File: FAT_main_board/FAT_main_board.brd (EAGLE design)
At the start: 335.3 x 178.7 mm, 42 parts, among them IC1 74LS241N

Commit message: [FAT board] Route board.
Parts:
- removed BAT_POWER1, BAT_POWER2, BAT_SIG1: (no value), con-ptr500:AK300/2
- added 12VSIG, POWER, POWER2: (no value), con-ptr500:AK300/2
- moved BAT_POWER 147.9 mm to (96.5, 1.27), turned to 180 degrees
- moved BAT_SIG 137.7 mm to (81.3, 1.27)
- moved BAU&INT 130.2 mm to (108.0, 1.27), turned to 180 degrees
- moved INTERRUPTOR 126.3 mm to (73.7, 16.5)
- moved BUCK_5V 107.6 mm to (41.9, 10.2), turned to 180 degrees
- moved HB3 85.9 mm to (20.3, 59.7), turned to 90 degrees
- moved C4 85.4 mm to (99.1, 58.4), turned to 0 degrees
- moved BUCK_10V 73.1 mm to (99.1, 29.2), turned to 90 degrees
- moved C6 63.2 mm to (26.7, 72.4), turned to 180 degrees
- moved C5 55.3 mm to (26.7, 47.0), turned to 0 degrees
- moved R3 45.8 mm to (41.9, 33.0), turned to 0 degrees
- moved DYN3 41.0 mm to (66.0, 29.2), turned to 90 degrees
- moved MOTOR3 40.7 mm to (36.8, 59.7), turned to 90 degrees
- moved JP2 40.6 mm to (52.1, 41.9), turned to 270 degrees
- moved DYN2 31.8 mm to (73.7, 29.2), turned to 90 degrees
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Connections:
- removed net N$22: BUCK_5V.IN+, INTERRUPTOR.1
- removed net N$23: BAT_POWER.2, BAT_POWER1.2, BAT_POWER2.2, BUCK_10V.IN-
- removed net N$25: BAT_SIG.2, BAT_SIG1.2, BUCK_5V.IN-
- new net 12V_SIG: 12VSIG.1, BUCK_5V.IN+, INTERRUPTOR.1
- net 12V_POWER: now also POWER.1, POWER2.1
- net GND: now also 12VSIG.2, BAT_POWER.2, BAT_SIG.2, BUCK_10V.IN-, BUCK_5V.IN-, POWER.2, POWER2.2
- net N$13: no longer BAT_POWER1.1, BAT_POWER2.1
- net N$18: now also SV2.8
- net N$20: no longer BAT_SIG1.1
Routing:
- net VCC: track 0.00 -> 366.5 mm, vias 0 -> 6
- net 12V_POWER: track 0.00 -> 292.1 mm
- net GND: track 0.00 -> 182.2 mm, vias 0 -> 13
- net MOT3_CURRENT: track 0.00 -> 108.0 mm, vias 0 -> 1
- net N$24: track 0.00 -> 98.6 mm, vias 0 -> 2
- net N$40: track 0.00 -> 55.8 mm
- net MOT3_BRK: track 0.00 -> 55.5 mm, vias 0 -> 1
- net MOT2_PWM: track 0.00 -> 49.0 mm, vias 0 -> 2
- net MOT2_BRK: track 0.00 -> 48.0 mm, vias 0 -> 2
- net N$8: track 0.00 -> 46.4 mm
- net MOT2_DIR: track 0.00 -> 46.2 mm, vias 0 -> 2
- net N$1: track 0.00 -> 43.7 mm, vias 0 -> 2
- net MOT2_CURRENT: track 0.00 -> 43.0 mm, vias 0 -> 2
- net MOT1_CURRENT: track 0.00 -> 42.7 mm
- net N$19: track 0.00 -> 42.5 mm
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- added copper zone on layer 16, net GND
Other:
- board size 335.3 x 178.7 mm -> 381 x 224.5 mm

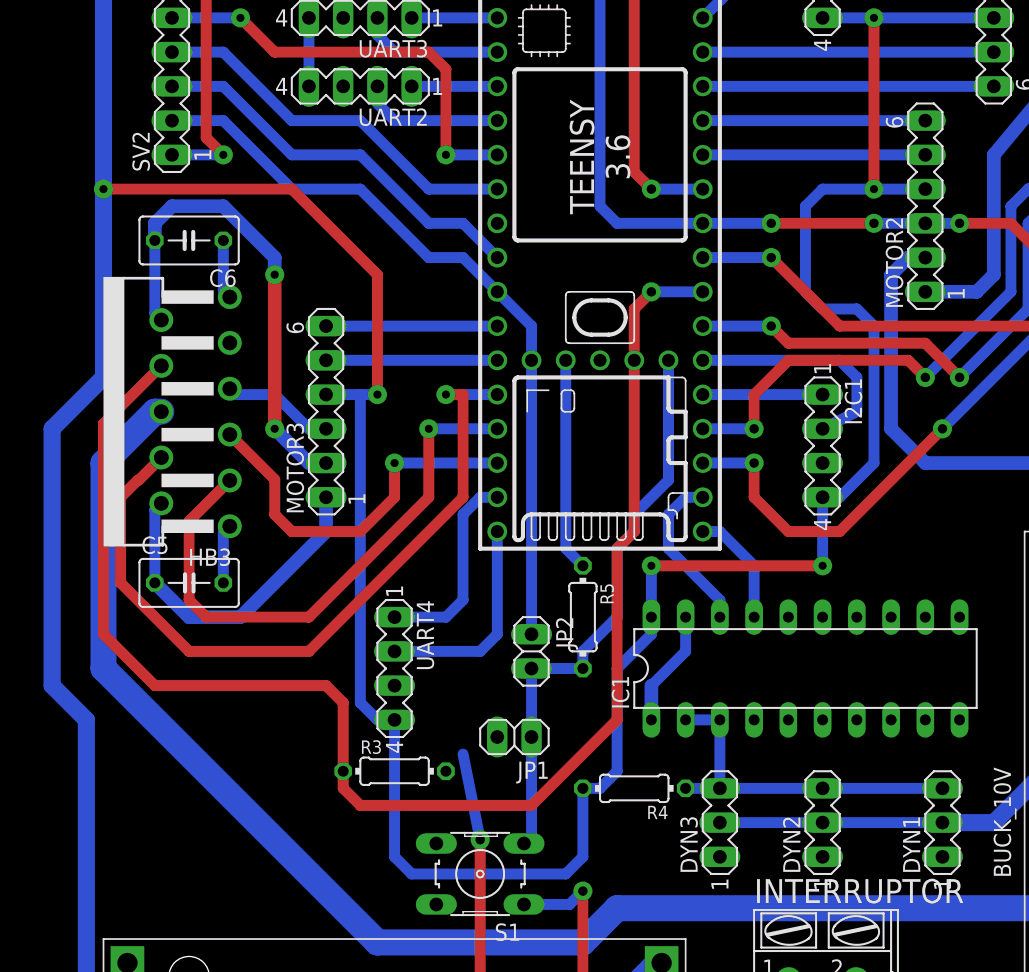
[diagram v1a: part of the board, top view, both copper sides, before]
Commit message: [FAT board] Modify board to match shematic correction.
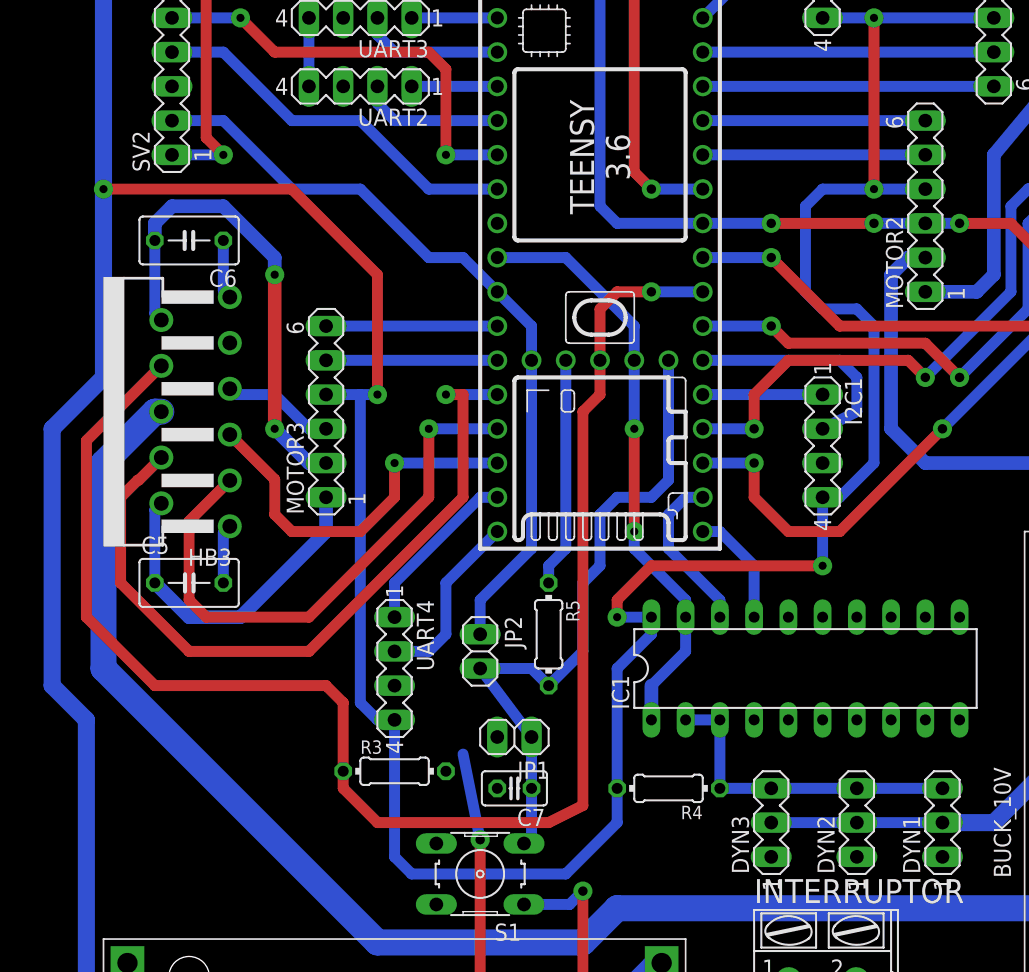
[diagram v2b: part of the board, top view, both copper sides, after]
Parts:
- added C7: (no value), rcl:C025-025X050
- moved JP2 3.81 mm to (48.3, 41.9)
- moved DYN3 3.81 mm to (69.8, 29.2)
- moved R5 2.84 mm to (53.3, 43.2)
- moved DYN2 2.54 mm to (76.2, 29.2)
- moved R4 2.54 mm to (62.2, 31.8)
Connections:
- removed net N$21: IC1.1, IC1.19
- removed net N$41: SV2.3, U$1.24
- new net DYN_DATA_CONTROL: IC1.1, IC1.19, U$1.24
- net GND: now also C7.2, U$1.AGND
- net N$19: now also C7.1
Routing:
- net DYN_DATA_CONTROL: track 0.00 -> 44.1 mm, vias 0 -> 2
- net N$41: track 29.4 -> 0.00 mm
- net N$21: track 8.67 -> 0.00 mm
- net N$19: track 42.5 -> 49.4 mm
- net MOT3_CURRENT: track 108.0 -> 113.6 mm
- net 10V_POWER: track 41.8 -> 38.0 mm
- net VCC: track 366.5 -> 369.3 mm
- net DYNA_DATA: track 26.7 -> 24.1 mm
- net RX4: track 15.0 -> 12.8 mm
- net TX4: track 15.8 -> 13.5 mm
- net N$40: track 55.8 -> 57.4 mm
- net N$26: track 15.8 -> 17.0 mm

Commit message: [FAT board] Adds some labels.
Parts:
- moved UART2 1.27 mm to (39.4, 82.5)
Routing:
- net N$11: track 32.1 -> 46.1 mm
- net VCC: track 369.3 -> 374.9 mm
- net N$12: track 28.3 -> 29.4 mm
- net TX2: track 10.7 -> 11.2 mm
- net RX2: track 6.35 -> 6.88 mm
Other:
- board size 381 x 224.5 mm -> 115.5 x 135.6 mm
- board text added: "11"
- board text added: "12"
- board text added: "13 (led)"
- board text added: "25"
- board text added: "5V"
- board text added: "BAU"
- board text added: "Dynamixels"
- board text added: "FAT board V1"
- board text added: "Fab @ ENAC - 2018"
- board text added: "GND"
- board text added: "I2C0"
- board text added: "I2C1"
- board text added: "I2C2"
- board text added: "Mot 1"
- board text added: "Mot 2"
- board text added: "Mot 3"
- board text added: "NC"
- board text added: "POW"
- board text added: "SIG"
- board text added: "U3"
- board text added: "UART1"
- board text added: "UART2"
- board text added: "UART4"
- board text added: "USB"
- board text added: "in +"
- board text added: "out +"
- board text added: "regu 5V"
- board text added: "régu 10V"
- board text added: "sig int"
- board text added: "~2"
- board text added: "~5"
- board text added: "~6"
